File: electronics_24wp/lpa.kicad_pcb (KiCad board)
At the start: 2 copper layers, 143 x 74 mm, 89 parts, among them IC1 ATMEGA328-A, P1 CONN_2, P2 CONN_3X2, U1 SD_CARD, U2 LD1117S33, U3 TLC5941, U4 TLC5941, U5 TLC5941, X1 CRYSTAL_SMD

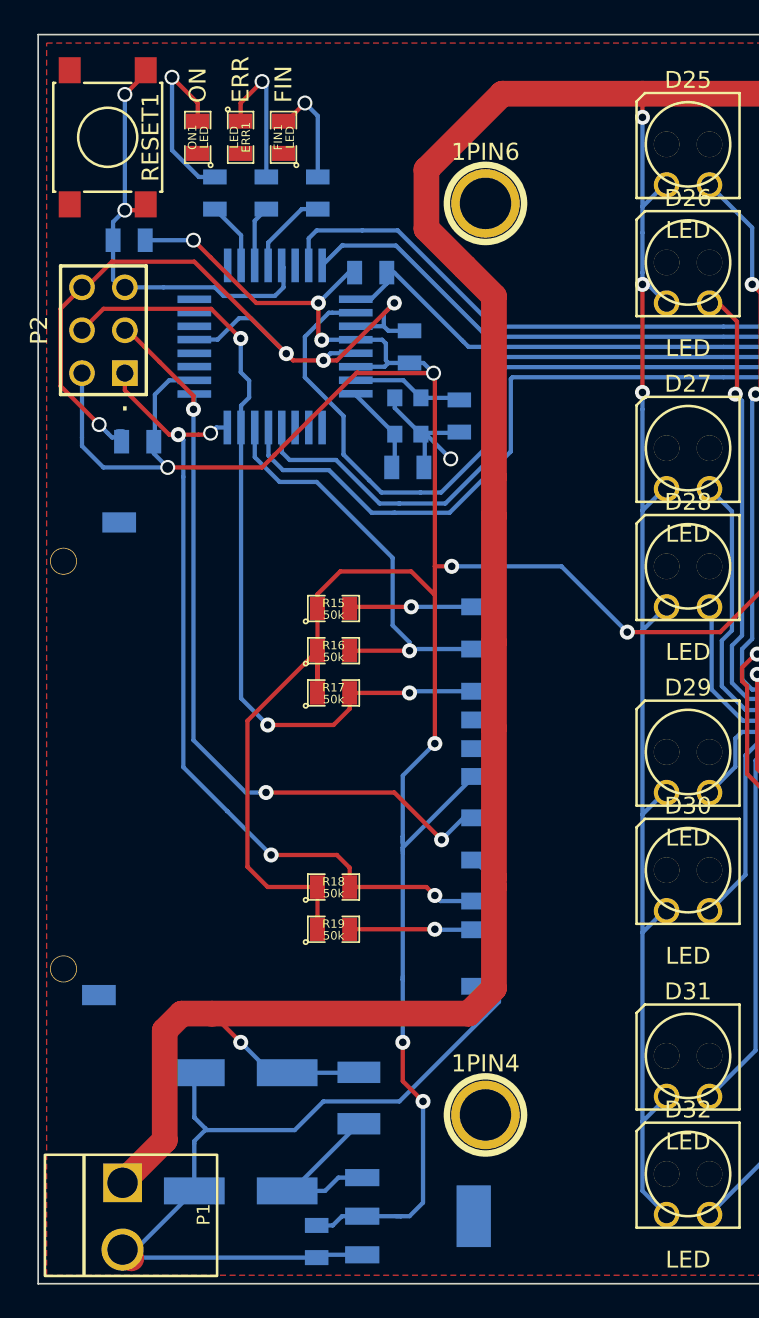
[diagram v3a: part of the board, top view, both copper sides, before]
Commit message: Removed pullup resistors from SD card socket.
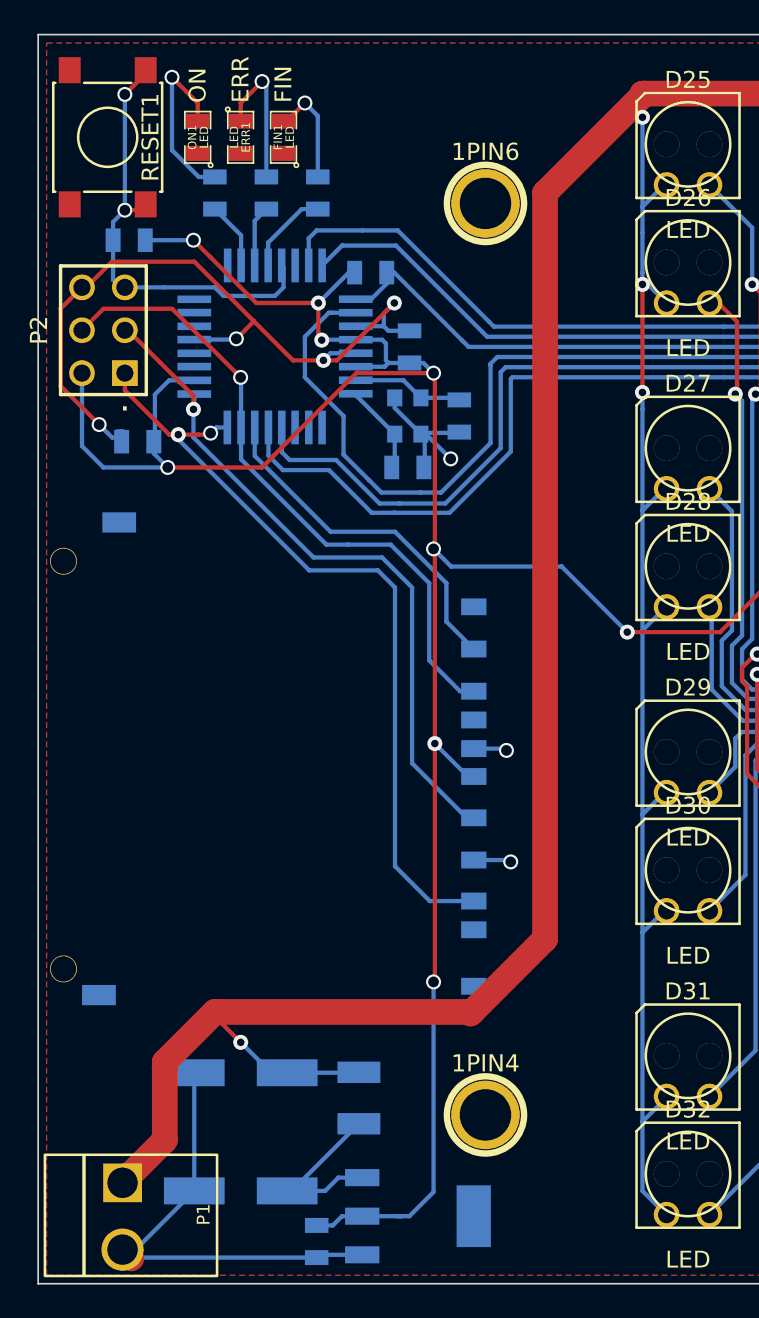
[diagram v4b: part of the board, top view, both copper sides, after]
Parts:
- removed R15, R16, R17, R18, R19: 50k, LPA_parts:SM0805
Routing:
- net /tlcs_1-3/VCC: track 310.3 -> 268.5 mm, vias 19 -> 18
- net GND: track 146.1 -> 108.8 mm, vias 8 -> 10
- net /MOSI: track 48.2 -> 38.6 mm, vias 3 -> 1
- net /tlcs_1-3/VIN: track 763.1 -> 753.5 mm
- net Net-(U1-Pad9): track 7.40 -> 0.00 mm, vias 1 -> 0
- net Net-(U1-Pad8): track 7.37 -> 0.00 mm, vias 1 -> 0
- net /SS: track 25.7 -> 20.7 mm, vias 1 -> 0
- net /SCK: track 46.6 -> 41.7 mm, vias 3 -> 1
- net /MISO: track 49.4 -> 47.1 mm, vias 4 -> 2

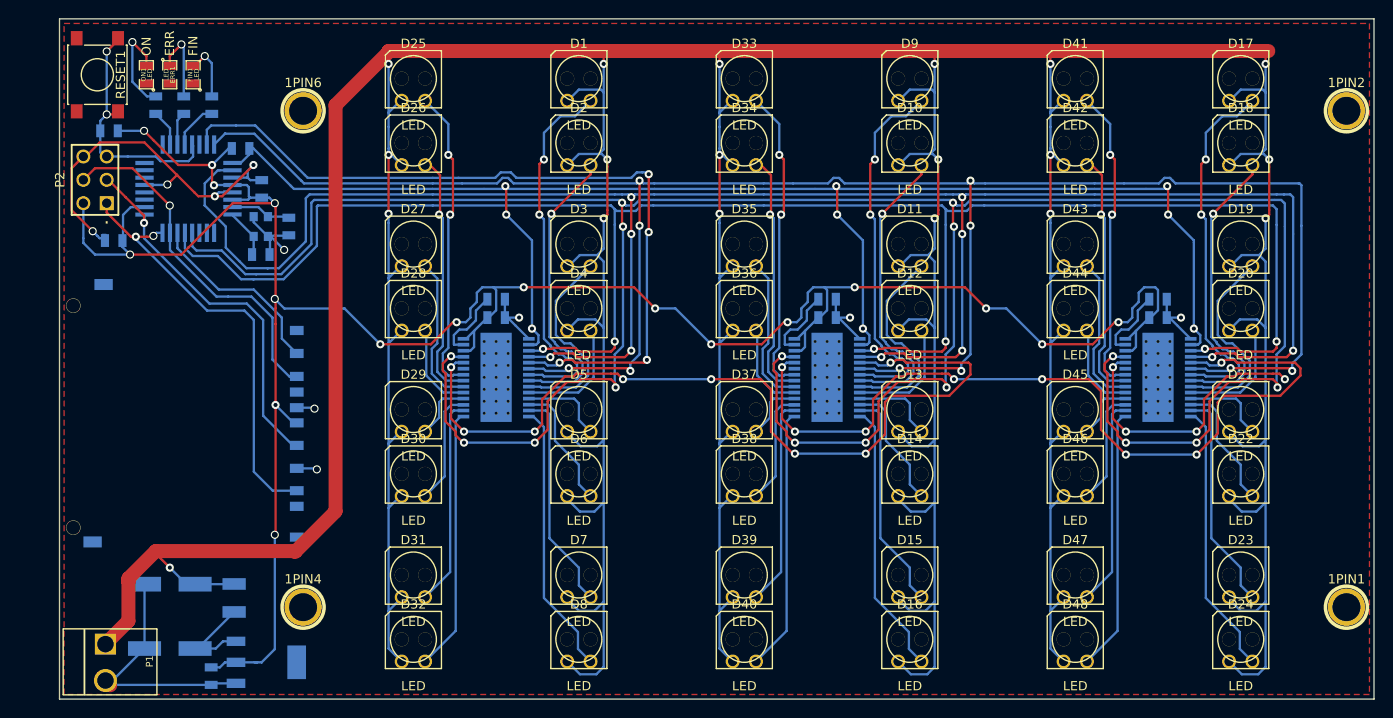
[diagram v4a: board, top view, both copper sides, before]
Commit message: Added one more decoupling resistor to uC.
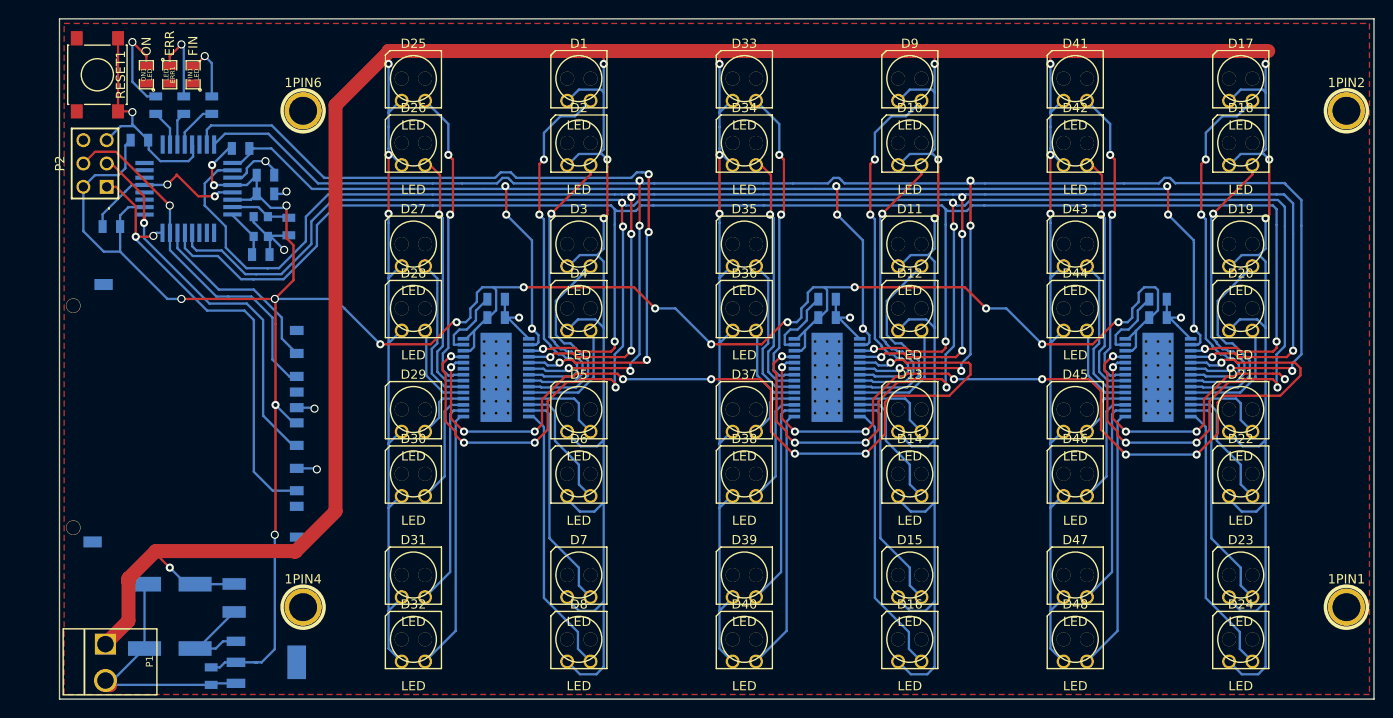
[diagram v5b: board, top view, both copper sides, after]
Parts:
- added C11: 0.1 uF, LPA_parts:SM0805, B.Cu at (89.4, 111.5)
- moved R1 3.45 mm to (75.7, 107.7), turned to 180 degrees
- moved P2 1.78 mm to (70.9, 110.2)
- moved C2 1.55 mm to (72.6, 117.1)
- moved C1 0.68 mm to (89.4, 113.5), turned to 180 degrees
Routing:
- net GND: track 108.8 -> 89.5 mm
- net /tlcs_1-3/VCC: track 268.5 -> 271.4 mm, vias 18 -> 17
- net /SCK: track 41.7 -> 44.5 mm
- net /MISO: track 47.1 -> 49.2 mm
- net /tlcs_1-3/SCLK: track 220.8 -> 219.2 mm
- net /tlcs_1-3/GSCLK: track 292.4 -> 290.9 mm
- net /tlcs_1-3/XLAT: track 204.2 -> 203.0 mm
- net /RST: track 26.6 -> 25.6 mm, vias 2 -> 1
- net /tlcs_1-3/MODE: track 220.1 -> 219.4 mm
- net /MOSI: track 38.6 -> 39.4 mm

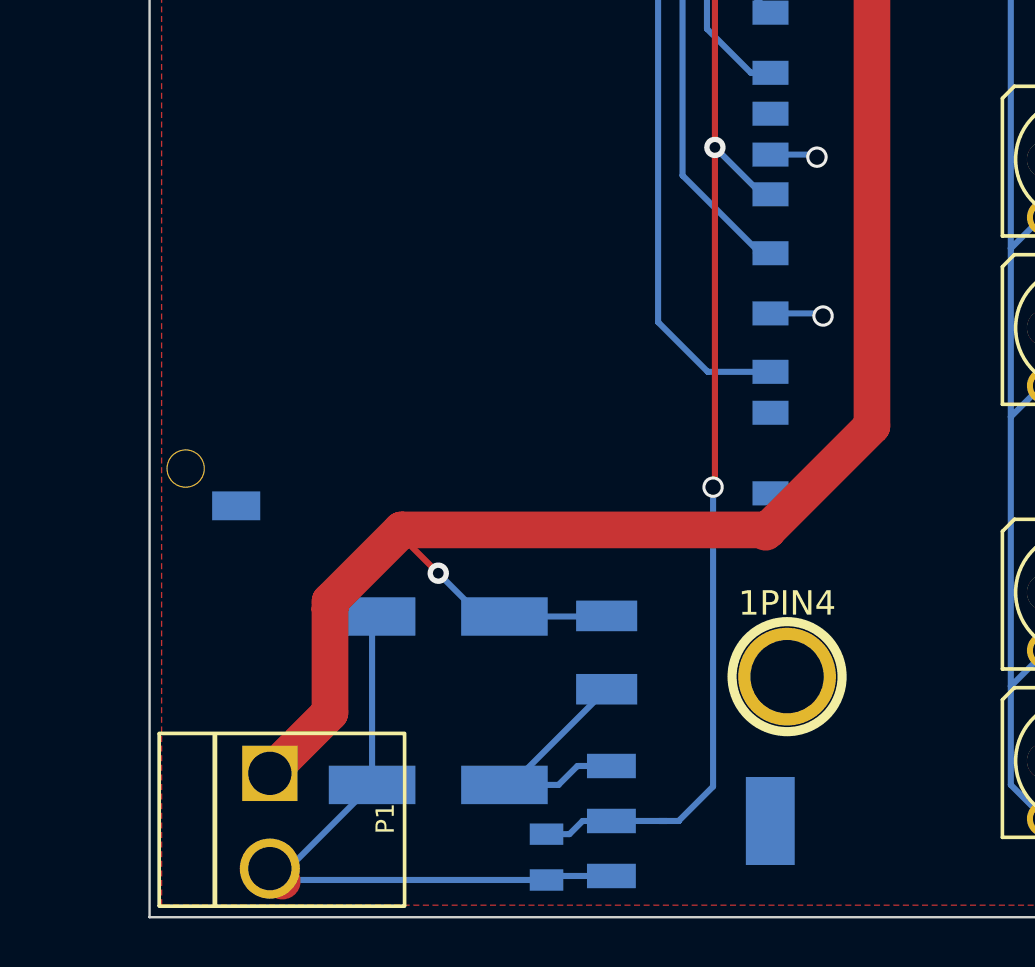
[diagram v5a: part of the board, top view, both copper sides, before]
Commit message: Replaced power connector by barrel jack.
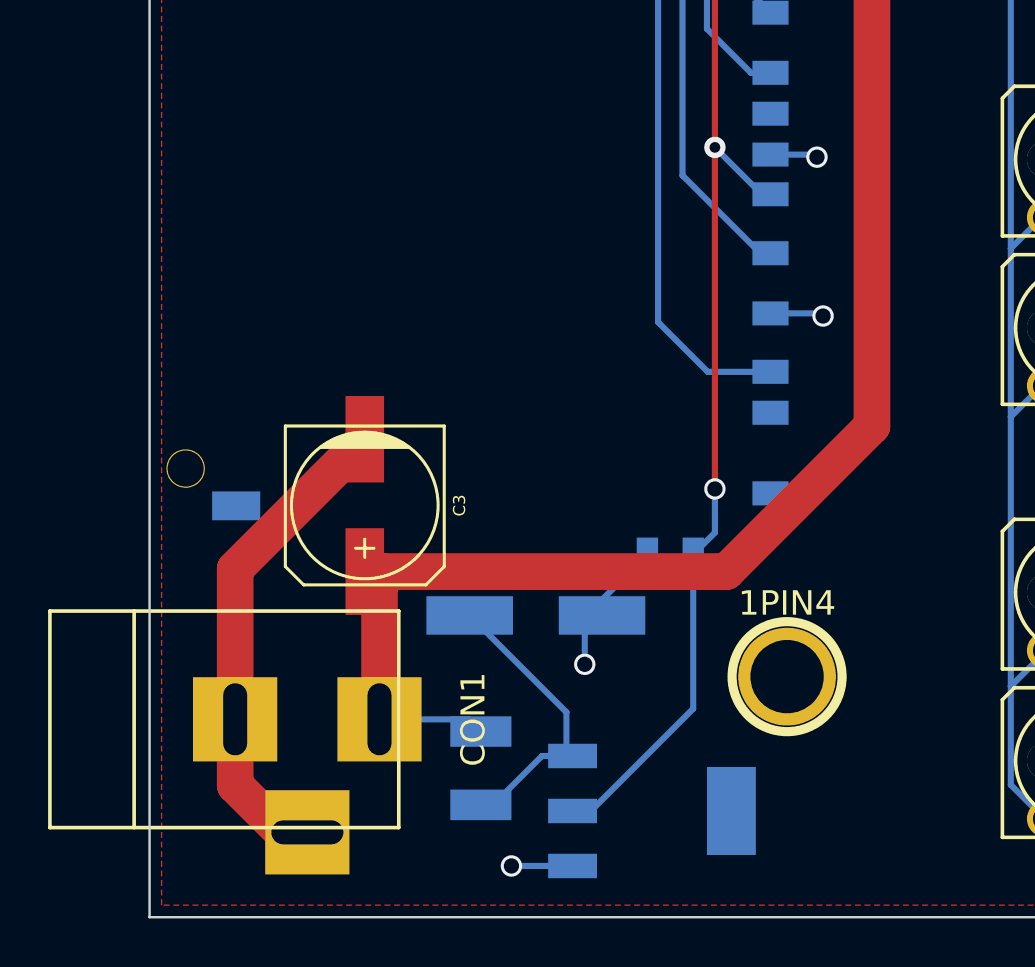
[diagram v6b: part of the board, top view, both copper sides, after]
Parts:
- removed P1: CONN_2, LPA_parts:CONNECTOR_2X1_3960um
- added CON1: BARREL_JACK, Connect:BARREL_JACK, F.Cu at (70.4, 160.3)
- C3: moved to F.Cu
- moved C5 13.6 mm to (88.6, 153.4), turned to 180 degrees
- moved C4 8.13 mm to (83.1, 156.0), turned to 180 degrees
- moved L1 7.10 mm to (80.8, 162.3)
- moved C3 5.53 mm to (75.9, 151.4), turned to 270 degrees
- moved U2 1.67 mm to (87.9, 164.1)
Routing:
- net /tlcs_1-3/VIN: track 753.5 -> 744.7 mm, vias 19 -> 18
- net /tlcs_1-3/VCC: track 271.4 -> 267.0 mm
- net Net-(C4-Pad1): track 10.9 -> 12.3 mm
- net GND: track 89.5 -> 90.5 mm, vias 10 -> 12

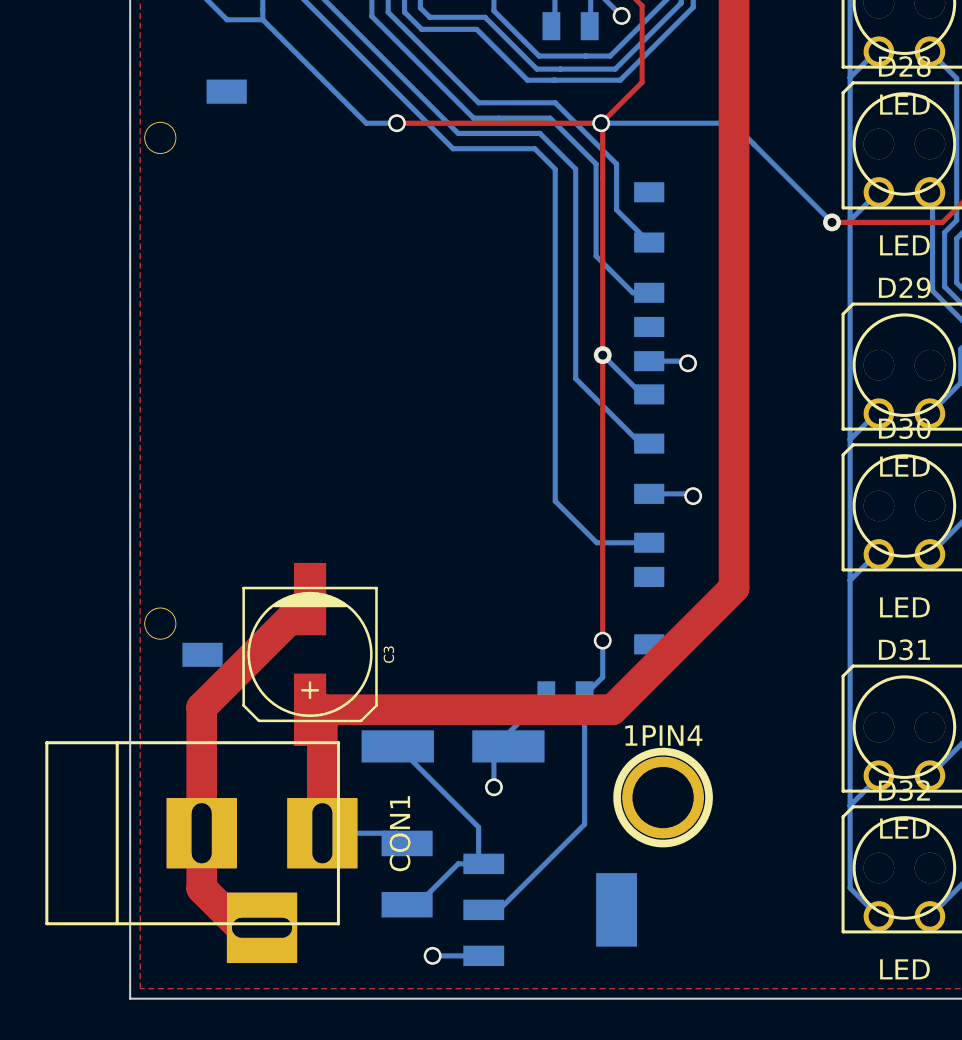
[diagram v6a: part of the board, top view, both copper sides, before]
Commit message: Changed power supply circuit.
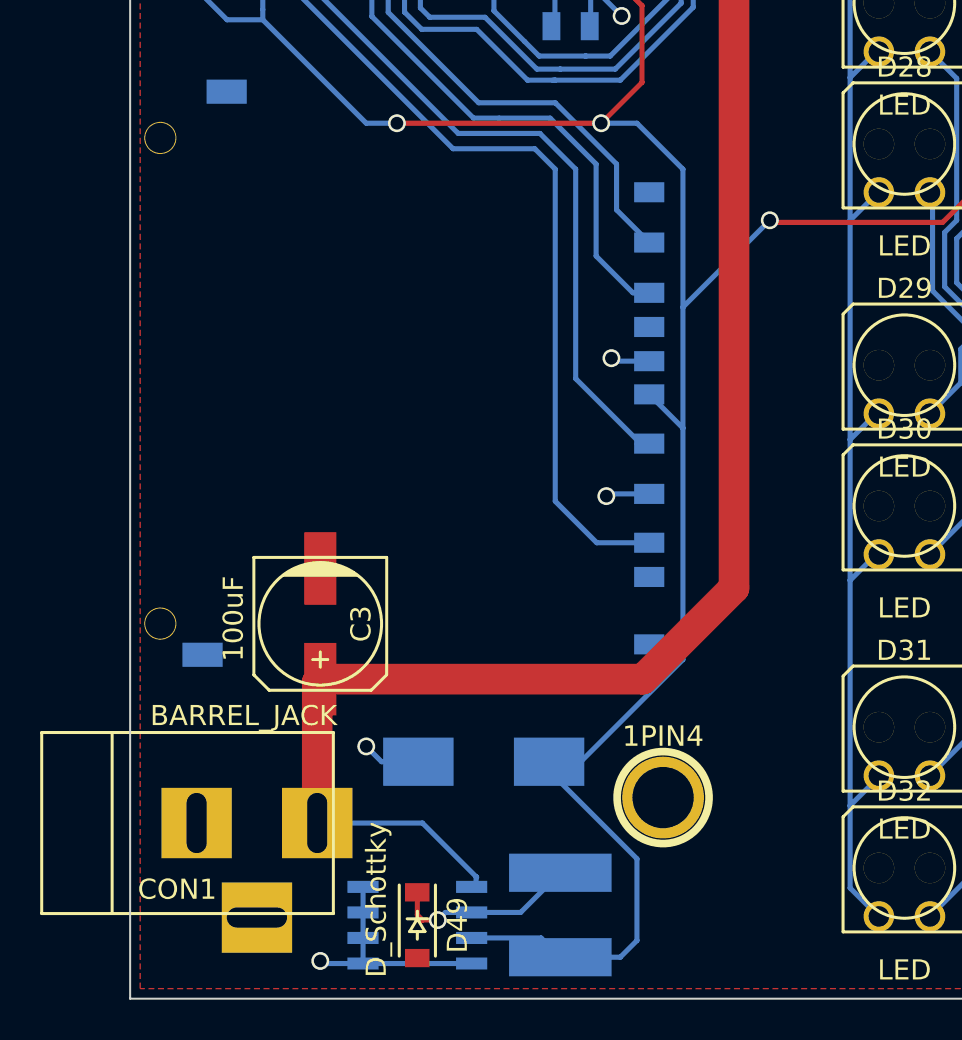
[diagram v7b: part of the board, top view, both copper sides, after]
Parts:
- removed C4: 47uF, c_elec_6.3x5.3
- added D49: D_Schottky, Diodes_SMD:SOD-123, F.Cu at (81.3, 164.8)
- C3: value 47uF -> 100uF; footprint c_elec_6.3x5.3 -> Capacitors_SMD:c_elec_6.3x7.7
- C5: value 10uF -> 470uF; footprint LPA_parts:SM0805 -> Capacitors_SMD:c_elec_8x10
- L1: value 10uH -> 150uH; footprint SM1210 -> LPA_parts:Inductor
- U2: value LD1117S33 -> AP1509; footprint SOT223 -> Housings_SOIC:SOIC-8_3.9x4.9mm_Pitch1.27mm
- moved L1 7.89 mm to (88.4, 164.3)
- moved U2 6.65 mm to (81.3, 164.8), turned to 180 degrees
- moved C5 5.24 mm to (84.6, 156.7), turned to 0 degrees
- moved C3 1.61 mm to (76.5, 149.9)
- moved CON1 0.57 mm to (70.1, 159.8)
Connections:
- L1 pad 1: /tlcs_1-3/VIN -> Net-(D49-Pad1)
- L1 pad 2: Net-(C4-Pad1) -> /tlcs_1-3/VCC
- U2 pad 1: GND -> /tlcs_1-3/VIN
- U2 pad 2: /tlcs_1-3/VCC -> Net-(D49-Pad1)
- U2 pad 3: Net-(C4-Pad1) -> /tlcs_1-3/VCC
- U2 pad 4: (no net) -> GND
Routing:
- net GND: track 90.5 -> 76.0 mm
- net Net-(C4-Pad1): track 12.3 -> 0.00 mm
- net /tlcs_1-3/VCC: track 267.0 -> 278.2 mm, vias 17 -> 15
- net Net-(D49-Pad1): track 0.00 -> 9.32 mm, vias 0 -> 1
- net /tlcs_1-3/VIN: track 744.7 -> 748.3 mm
